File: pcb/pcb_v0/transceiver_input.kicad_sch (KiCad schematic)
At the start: 25 parts, among them U2 LM324

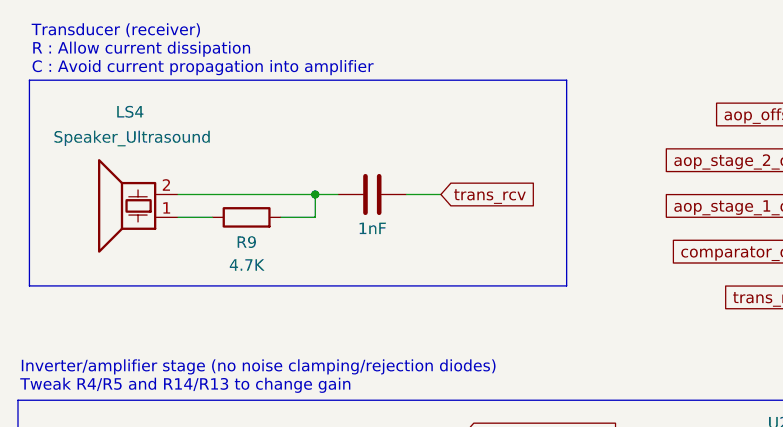
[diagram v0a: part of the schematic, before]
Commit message: fix(pcb): update design to match teacher requirements
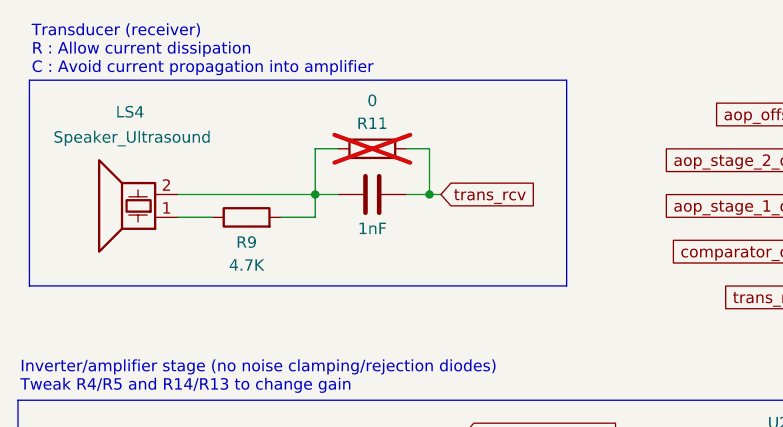
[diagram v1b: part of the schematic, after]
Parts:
- added R11: 0, Resistor_THT:R_Axial_DIN0207_L6.3mm_D2.5mm_P10.16mm_Horizontal, symbol Device:R
- C10, C2, C3: footprint Capacitor_THT:C_Disc_D3.0mm_W1.6mm_P2.50mm -> Capacitor_THT:C_Disc_D4.3mm_W1.9mm_P5.00mm
- R1, R10, R14, R2, R4, R5, R6, R7, R8, R9: footprint Resistor_THT:R_Axial_DIN0204_L3.6mm_D1.6mm_P5.08mm_Horizontal -> Resistor_THT:R_Axial_DIN0207_L6.3mm_D2.5mm_P10.16mm_Horizontal
- TP10, TP11, TP13, TP14, TP6, TP7, TP8, TP9: footprint TestPoint:TestPoint_THTPad_1.0x1.0mm_Drill0.5mm -> TestPoint:TestPoint_THTPad_3.0x3.0mm_Drill1.5mm
- U2: footprint Package_DIP:DIP-14_W7.62mm_Socket_LongPads -> LM324AN:N14
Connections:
- net trans_rcv: now also R11.1
- net at C10.1, LS4.2, R9.2: now also R11.2
